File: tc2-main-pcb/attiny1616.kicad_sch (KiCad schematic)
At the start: 21 parts, among them SW101 SW_Push, U117 ATtiny1616-M

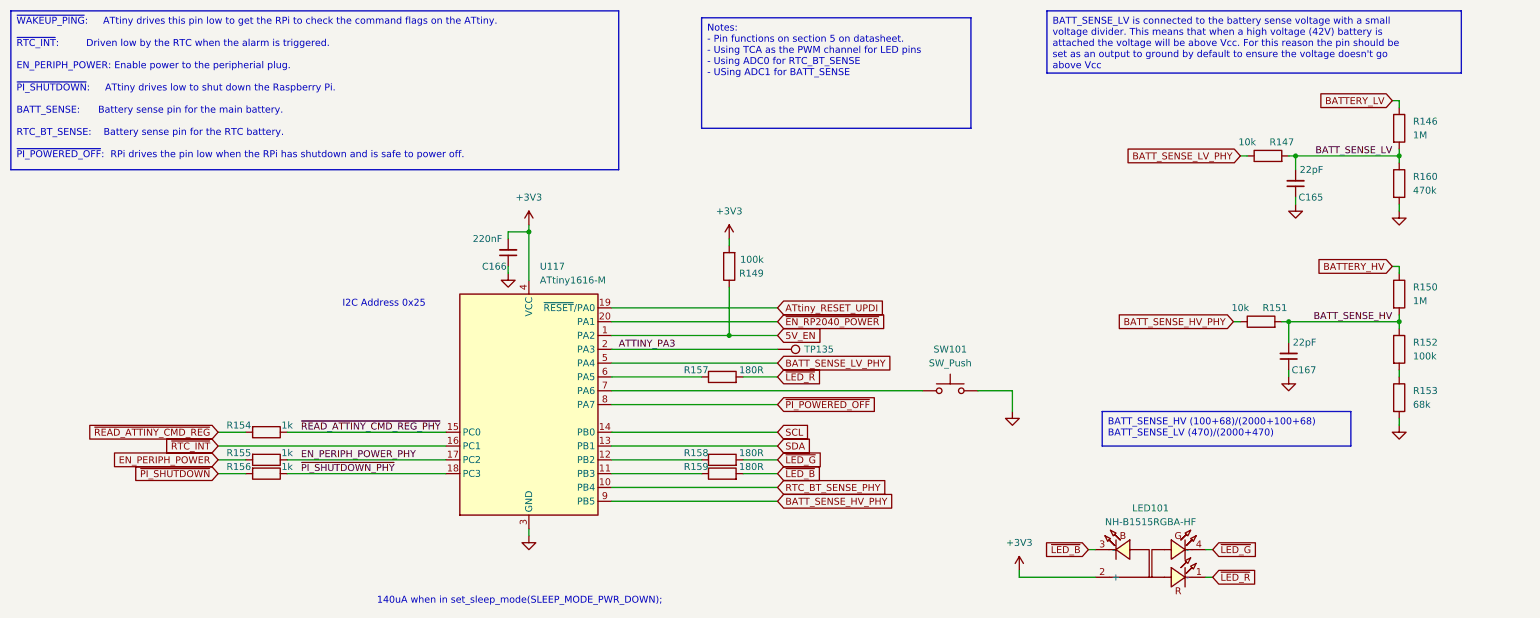
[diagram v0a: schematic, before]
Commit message: Upgraded to new kicad version
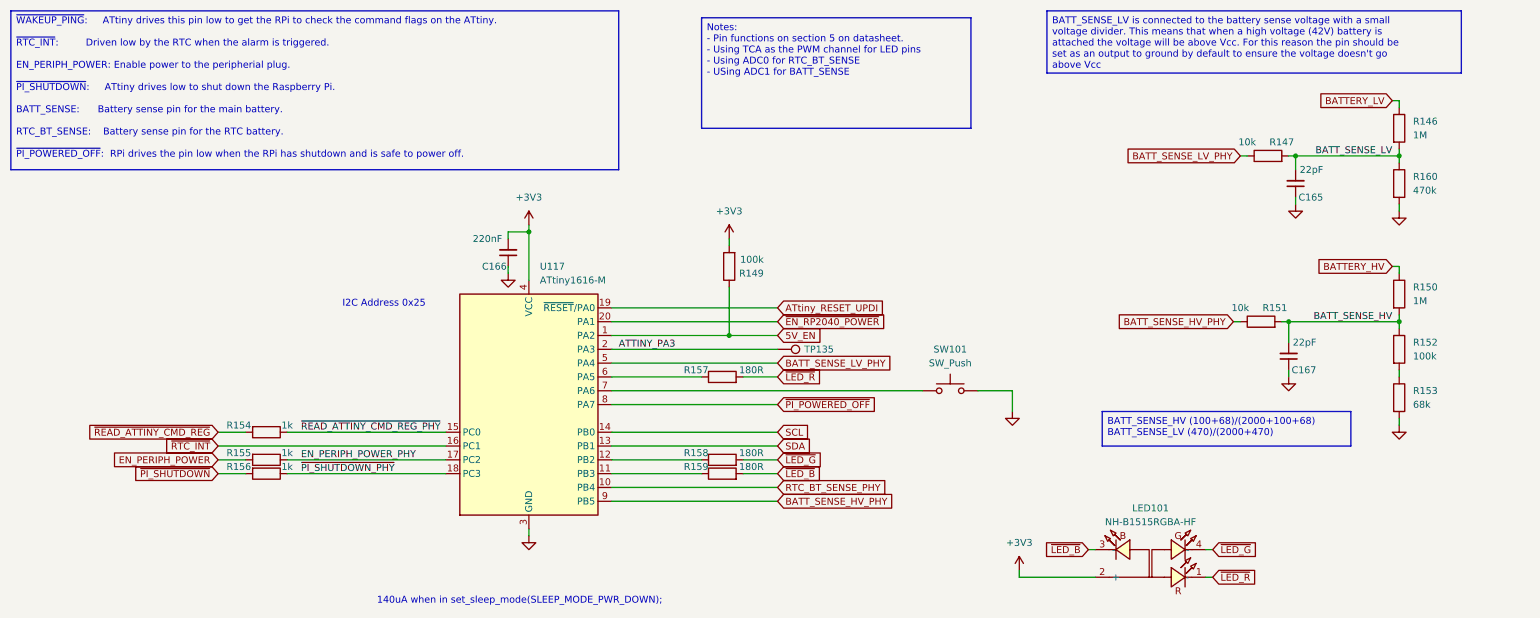
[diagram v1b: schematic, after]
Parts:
- U117: footprint Package_DFN_QFN:VQFN-20-1EP_3x3mm_P0.4mm_EP1.7x1.7mm -> cacophony-library:VQFN-20-1EP_3x3mm_P0.4mm_EP1.7x1.7mm
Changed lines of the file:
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@@
 (kicad_sch
-	(version 20231120)
+	(version 20250114)
 	(generator "eeschema")
-	(generator_version "8.0")
+	(generator_version "9.0")
 	(paper "A4")
+	(text "140uA when in set_sleep_mode(SLEEP_MODE_PWR_DOWN);"
+		(exclude_from_sim no)
+		(at 82.55 156.21 0)
+		(effects
+			(font
+				(size 1.27 1.27)
+			)
+			(justify left bottom)
+		)
+	)
+	(text "I2C Address 0x25"
+		(exclude_from_sim no)
+		(at 76.2 101.6 0)
+		(effects
+			(font
+				(size 1.27 1.27)
+			)
+			(justify left bottom)
+		)
+	)
+	(text_box "BATT_SENSE_LV is connected to the battery sense voltage with a small voltage divider. This means that when a high voltage (42V) battery is attached the voltage will be above Vcc. For this reason the pin should be set as an output to ground by default to ensure the voltage doesn't go above Vcc"
+		(exclude_from_sim no)
+		(at 205.74 46.99 0)
+		(size 76.2 11.43)
+		(margins 0.9525 0.9525 0.9525 0.9525)
+		(stroke
+			(width 0)
+			(type default)
+		)
+		(fill
+			(type color)
+			(color 255 229 191 1)
+		)
+		(effects
+			(font
+				(size 1.27 1.27)
+			)
+			(justify left top)
+		)
+	)
+	(text_box "BATT_SENSE_HV (100+68)/(2000+100+68)\nBATT_SENSE_LV (470)/(2000+470)"
+		(exclude_from_sim no)
+		(at 215.9 120.65 0)
+		(size 45.72 6.35)
+		(margins 0.9525 0.9525 0.9525 0.9525)
+		(stroke
+			(width 0)
+			(type default)
+		)
+		(fill
+			(type color)
+			(color 255 229 191 1)
+		)
+		(effects
+			(font
+				(size 1.27 1.27)
+			)
+			(justify left top)
+		)
+	)
+	(text_box "~{WAKEUP_PING}:     ATtiny drives this pin low to get the RPi to check the command flags on the ATtiny.\n\n~{RTC_INT}:         Driven low by the RTC when the alarm is triggered.\n\nEN_PERIPH_POWER: Enable power to the peripherial plug.\n\n~{PI_SHUTDOWN}:     ATtiny drives low to shut down the Raspberry Pi.\n\nBATT_SENSE:      Battery sense pin for the main battery.\n\nRTC_BT_SENSE:    Battery sense pin for the RTC battery.\n\n~{PI_POWERED_OFF}:  RPi drives the pin low when the RPi has shutdown and is safe to power off."
+		(exclude_from_sim no)
+		(at 15.24 46.99 0)
+		(size 111.76 29.21)
+		(margins 0.9525 0.9525 0.9525 0.9525)
+		(stroke
+			(width 0)
+			(type default)
+		)
+		(fill
+			(type color)
+			(color 255 229 191 1)
+		)
+		(effects
+			(font
+				(face "DejaVu Sans Mono")
+				(size 1.27 1.27)
+			)
+			(justify left top)
+		)
+	)
+	(text_box "Notes:\n- Pin functions on section 5 on datasheet.\n- Using TCA as the PWM channel for LED pins\n- Using ADC0 for RTC_BT_SENSE\n- USing ADC1 for BATT_SENSE"
+		(exclude_from_sim no)
+		(at 142.24 48.26 0)
+		(size 49.53 20.32)
+		(margins 0.9525 0.9525 0.9525 0.9525)
+		(stroke
+			(width 0)
+			(type default)
+		)
+		(fill
+			(type color)
+			(color 255 229 191 1)
+		)
+		(effects
+			(font
+				(size 1.27 1.27)
+			)
+			(justify left top)
+		)
+	)
 	(junction
 		(at 147.32 106.68)
@@
 		)
 	)
-	(text_box "BATT_SENSE_LV is connected to the battery sense voltage with a small voltage divider. This means that when a high voltage (42V) battery is attached the voltage will be above Vcc. For this reason the pin should be set as an output to ground by default to ensure the voltage doesn't go above Vcc"
-		(exclude_from_sim no)
-		(at 205.74 46.99 0)
-		(size 76.2 11.43)
-		(stroke
-			(width 0)
-			(type default)
-		)
-		(fill
-			(type color)
-			(color 255 229 191 1)
-		)
-		(effects
-			(font
-				(size 1.27 1.27)
-			)
-			(justify left top)
-		)
-	)
-	(text_box "BATT_SENSE_HV (100+68)/(2000+100+68)\nBATT_SENSE_LV (470)/(2000+470)"
-		(exclude_from_sim no)
-		(at 215.9 120.65 0)
-		(size 45.72 6.35)
-		(stroke
-			(width 0)
-			(type default)
-		)
-		(fill
-			(type color)
-			(color 255 229 191 1)
-		)
-		(effects
-			(font
-				(size 1.27 1.27)
-			)
-			(justify left top)
-		)
-	)
-	(text_box "~{WAKEUP_PING}:     ATtiny drives this pin low to get the RPi to check the command flags on the ATtiny.\n\n~{RTC_INT}:         Driven low by the RTC when the alarm is triggered.\n\nEN_PERIPH_POWER: Enable power to the peripherial plug.\n\n~{PI_SHUTDOWN}:     ATtiny drives low to shut down the Raspberry Pi.\n\nBATT_SENSE:      Battery sense pin for the main battery.\n\nRTC_BT_SENSE:    Battery sense pin for the RTC battery.\n\n~{PI_POWERED_OFF}:  RPi drives the pin low when the RPi has shutdown and is safe to power off."
-		(exclude_from_sim no)
-		(at 15.24 46.99 0)
-		(size 111.76 29.21)
-		(stroke
-			(width 0)
-			(type default)
-		)
-		(fill
-			(type color)
-			(color 255 229 191 1)
-		)
-		(effects
-			(font
-				(face "DejaVu Sans Mono")
-				(size 1.27 1.27)
-			)
-			(justify left top)
-		)
-	)
-	(text_box "Notes:\n- Pin functions on section 5 on datasheet.\n- Using TCA as the PWM channel for LED pins\n- Using ADC0 for RTC_BT_SENSE\n- USing ADC1 for BATT_SENSE"
-		(exclude_from_sim no)
-		(at 142.24 48.26 0)
-		(size 49.53 20.32)
-		(stroke
-			(width 0)
-			(type default)
-		)
-		(fill
-			(type color)
-			(color 255 229 191 1)
-		)
-		(effects
-			(font
-				(size 1.27 1.27)
-			)
-			(justify left top)
-		)
-	)
-	(text "140uA when in set_sleep_mode(SLEEP_MODE_PWR_DOWN);"
-		(exclude_from_sim no)
-		(at 82.55 156.21 0)
-		(effects
-			(font
-				(size 1.27 1.27)
-			)
-			(justify left bottom)
-		)
-	)
-	(text "I2C Address 0x25"
-		(exclude_from_sim no)
-		(at 76.2 101.6 0)
-		(effects
-			(font
-				(size 1.27 1.27)
-			)
-			(justify left bottom)
-		)
-	)
 	(label "BATT_SENSE_HV"
 		(at 269.24 104.14 180)
-		(fields_autoplaced yes)
 		(effects
 			(font
@@
 	(label "~{PI_SHUTDOWN_PHY}"
 		(at 68.58 132.08 0)
-		(fields_autoplaced yes)
 		(effects
 			(font
@@
 	(label "BATT_SENSE_LV"
 		(at 269.24 73.66 180)
-		(fields_autoplaced yes)
 		(effects
 			(font
@@
 	(label "ATTINY_PA3"
 		(at 127 109.22 0)
-		(fields_autoplaced yes)
 		(effects
 			(font
@@
 	(label "~{READ_ATTINY_CMD_REG_PHY}"
 		(at 68.58 124.46 0)
-		(fields_autoplaced yes)
 		(effects
 			(font
@@
 	(label "EN_PERIPH_POWER_PHY"
 		(at 68.58 129.54 0)
-		(fields_autoplaced yes)
 		(effects
 			(font
@@
 			)
 		)
-		(property "Footprint" "Package_DFN_QFN:VQFN-20-1EP_3x3mm_P0.4mm_EP1.7x1.7mm"
+		(property "Footprint" "cacophony-library:VQFN-20-1EP_3x3mm_P0.4mm_EP1.7x1.7mm"
 			(at 110.49 119.38 0)
 			(effects

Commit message: Tidy up for making an order for v0.7.3
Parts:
- C165, C167: LCSC C1555 -> (none); LCSC Part (none) -> C1555
- C166: LCSC C16772 -> (none); LCSC Part (none) -> C16772
- LED101: LCSC C2874115 -> (none); LCSC Part (none) -> C2874115
- R146, R150: LCSC C326730 -> (none); LCSC Part (none) -> C326730
- R147, R151: LCSC C25744 -> (none); LCSC Part (none) -> C25744
- R149: LCSC C25741 -> (none); LCSC Part (none) -> C25741
- R152: LCSC C445619 -> (none); LCSC Part (none) -> C445619
- R153: LCSC C445618 -> (none); LCSC Part (none) -> C445618
- R154, R155, R156: LCSC C11702 -> (none); LCSC Part (none) -> C11702
- R157, R158, R159: value 180R -> 180Ω; LCSC C38941 -> (none); LCSC Part (none) -> C38941
- R160: LCSC C319591 -> (none); LCSC Part (none) -> C319591
- SW101: LCSC C4364951 -> (none); LCSC Part (none) -> C4364951
- U117: LCSC C507118 -> (none); LCSC Part (none) -> C507118
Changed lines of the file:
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@@
 			)
 		)
-		(property "LCSC" "C326730"
+		(property "LCSC Part" "C326730"
 			(at 270.51 99.06 0)
 			(effects
@@
 			)
 		)
-		(property "LCSC" "C445618"
+		(property "LCSC Part" "C445618"
 			(at 270.51 118.11 0)
 			(effects
@@
 			)
 		)
-		(property "LCSC" "C11702"
+		(property "LCSC Part" "C11702"
 			(at 62.23 129.54 0)
 			(effects
@@
 			)
 		)
-		(property "LCSC" "C326730"
+		(property "LCSC Part" "C326730"
 			(at 270.51 68.58 0)
 			(effects
@@
 			)
 		)
-		(property "LCSC" "C11702"
+		(property "LCSC Part" "C11702"
 			(at 62.23 124.46 0)
 			(effects
@@
 			)
 		)
-		(property "Value" "180R"
+		(property "Value" "180Ω"
 			(at 153.67 113.03 90)
 			(effects
@@
 			)
 		)
-		(property "LCSC" "C38941"
+		(property "LCSC Part" "C38941"
 			(at 146.05 114.3 0)
 			(effects
@@
 			)
 		)
-		(property "LCSC" "C445619"
+		(property "LCSC Part" "C445619"
 			(at 270.51 109.22 0)
 			(effects
@@
 			)
 		)
-		(property "LCSC" "C1555"
+		(property "LCSC Part" "C1555"
 			(at 250.19 110.49 0)
 			(effects
@@
 			)
 		)
-		(property "LCSC" "C25744"
+		(property "LCSC Part" "C25744"
 			(at 246.38 73.66 0)
 			(effects
@@
 			)
 		)
-		(property "Value" "180R"
+		(property "Value" "180Ω"
 			(at 153.67 128.27 90)
 			(effects
@@
 			)
 		)
-		(property "LCSC" "C38941"
+		(property "LCSC Part" "C38941"
 			(at 146.05 129.54 0)
 			(effects
@@
 			)
 		)
-		(property "LCSC" "C4364951"
+		(property "LCSC Part" "C4364951"
 			(at 187.96 116.84 0)
 			(effects
@@
 			)
 		)
-		(property "Value" "180R"
+		(property "Value" "180Ω"
 			(at 153.67 130.81 90)
 			(effects
@@
 			)
 		)
-		(property "LCSC" "C38941"
+		(property "LCSC Part" "C38941"
 			(at 146.05 132.08 0)
 			(effects
@@
 			)
 		)
-		(property "LCSC" "C25744"
+		(property "LCSC Part" "C25744"
 			(at 245.11 104.14 0)
 			(effects
@@
 			)
 		)
-		(property "LCSC" "C25741"
+		(property "LCSC Part" "C25741"
 			(at 147.32 93.98 0)
 			(effects
@@
 			)
 		)
-		(property "LCSC Part" ""
+		(property "LCSC Part" "C2874115"
 			(at 224.79 163.83 0)
 			(effects
@@
 			)
 		)
-		(property "LCSC" "C2874115"
-			(at 224.79 148.59 0)
-			(effects
-				(font
-					(size 1.27 1.27)
-				)
-				(hide yes)
-			)
-		)
 		(pin "1"
 		)
@@
 			)
 		)
-		(property "LCSC" "C16772"
+		(property "LCSC Part" "C16772"
 			(at 106.68 91.44 0)
 			(effects
@@
 			)
 		)
-		(property "LCSC" "C11702"
+		(property "LCSC Part" "C11702"
 			(at 62.23 132.08 0)
 			(effects
@@
 			)
 		)
-		(property "LCSC" "C1555"
+		(property "LCSC Part" "C1555"
 			(at 251.46 78.74 0)
 			(effects
@@
 			)
 		)
-		(property "LCSC" "C319591"
+		(property "LCSC Part" "C319591"
 			(at 270.51 78.74 0)
 			(effects
@@
 			)
 		)
-		(property "LCSC" "C507118"
+		(property "LCSC Part" "C507118"
 			(at 110.49 119.38 0)
 			(effects
